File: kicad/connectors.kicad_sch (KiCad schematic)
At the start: 3 parts, among them J2 Conn_02x05_Odd_Even, J3 Conn_01x05, J4 Conn_01x05

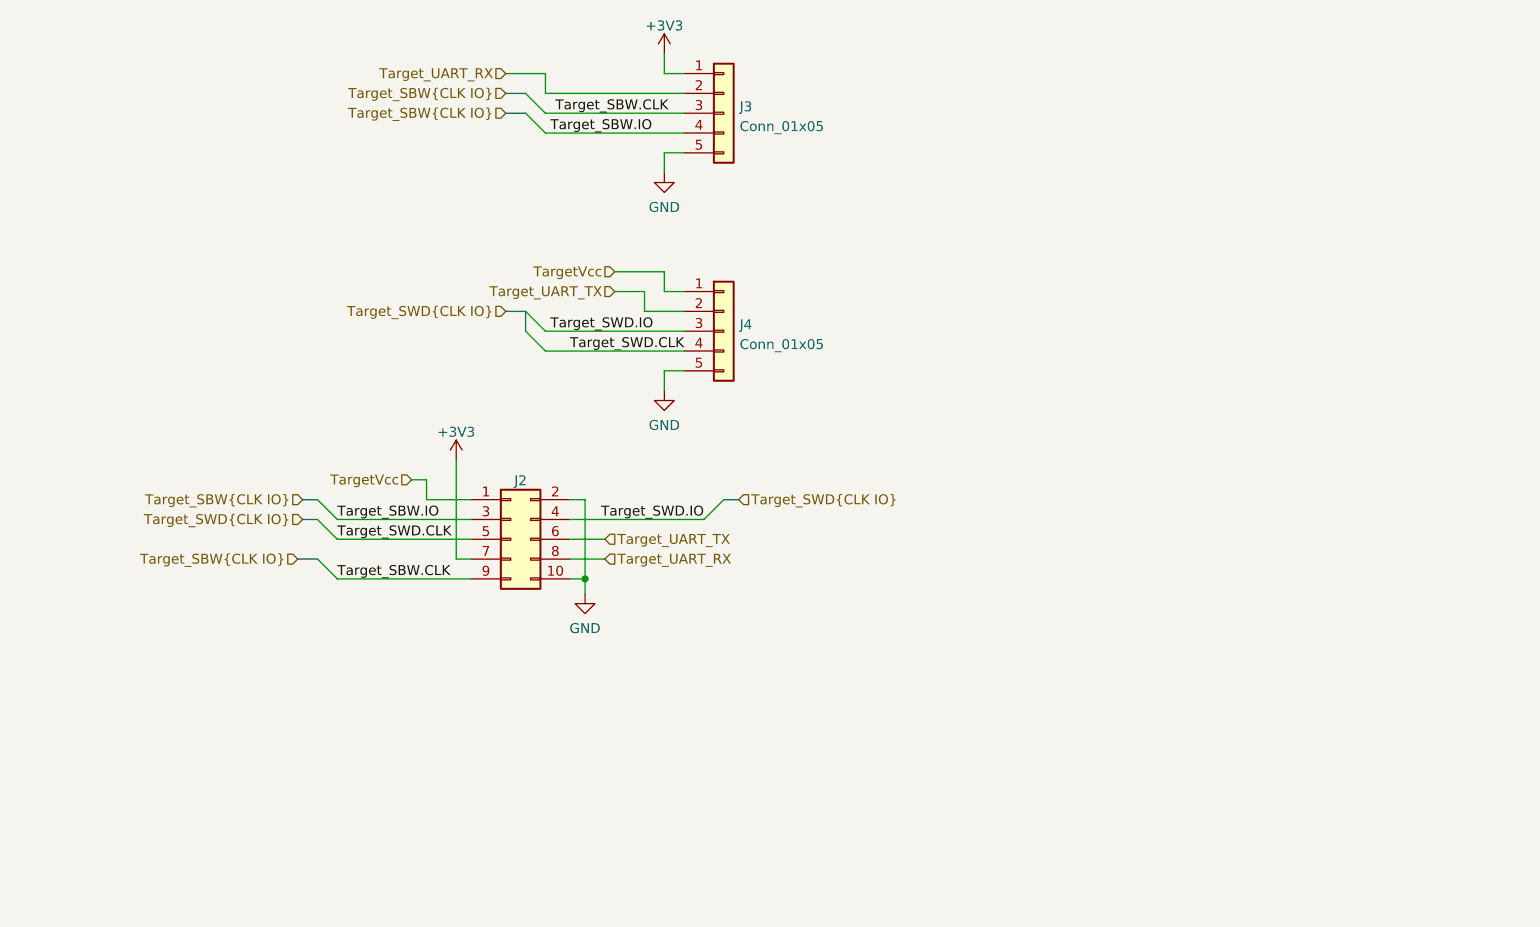
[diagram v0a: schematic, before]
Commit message: add fourth level converter for simultaneous programming + TX/RX
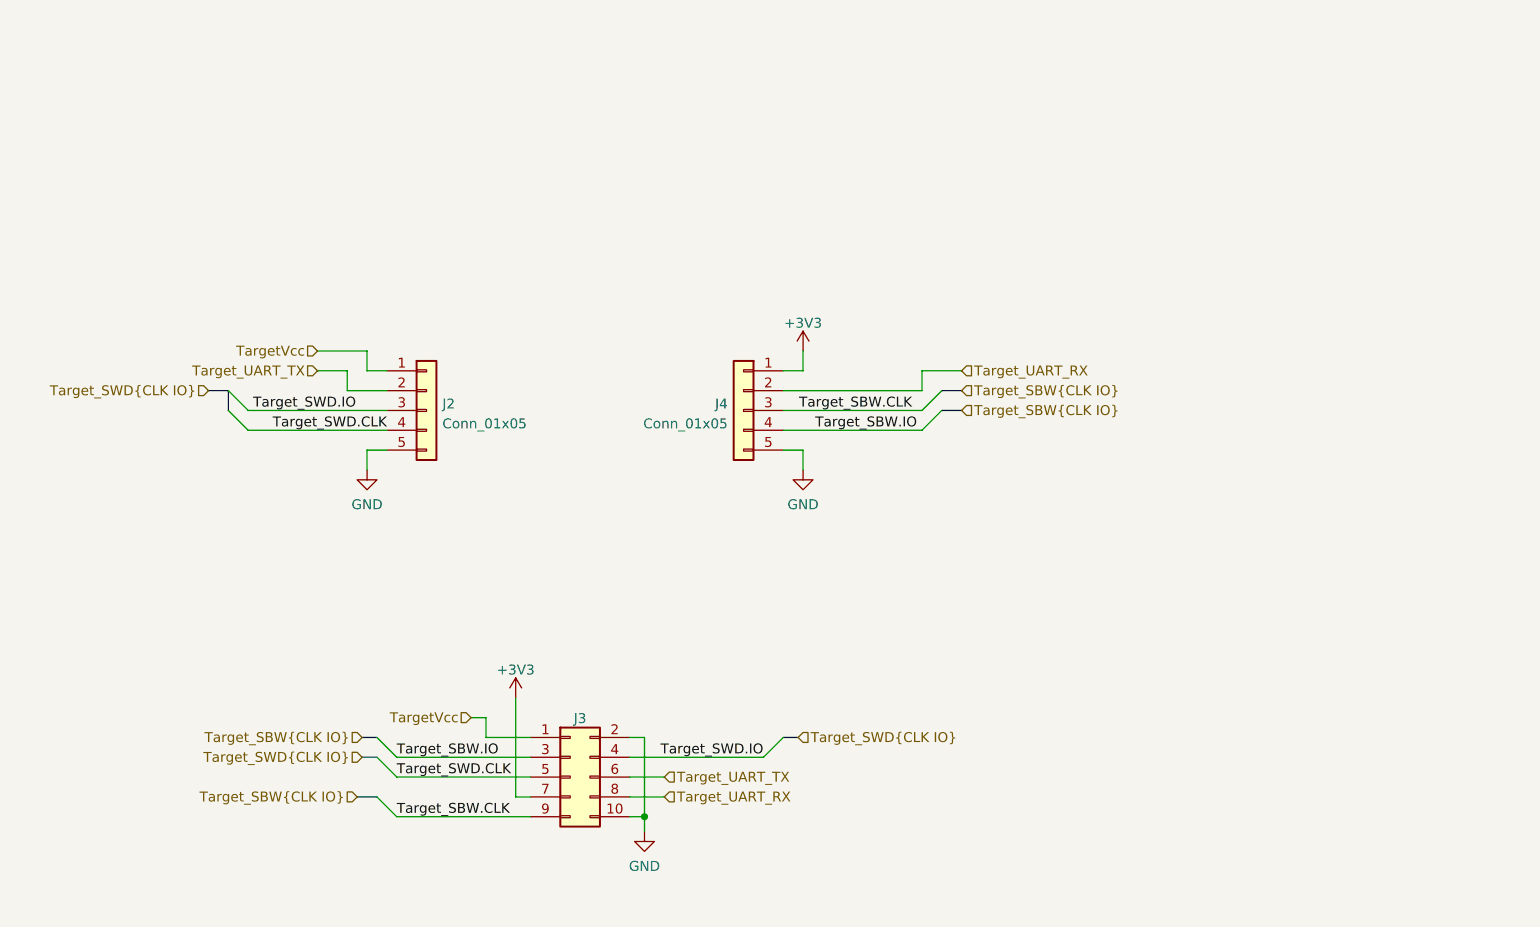
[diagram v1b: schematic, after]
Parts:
- renumbered J4 to J2, J2 to J3, J3 to J4
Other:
- moved on the sheet: J2, J3, J4

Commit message: replace target supply diode with analog switch
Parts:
- removed J2, J4: Conn_01x05, riotee:PinHeader_1x05_P2.54mm_Plain, symbol Connector_Generic:Conn_01x05
- added C28: 0.1u, Capacitor_SMD:C_0402_1005Metric, symbol Device:C
- added J2, J4: Conn_01x07, riotee:PinHeader_1x07_P2.54mm_Plain, symbol Connector_Generic:Conn_01x07
- added R27: 12R, Resistor_SMD:R_0402_1005Metric, symbol Device:R
- added U9: TS5A3166YZP, riotee:TI_YZP0005, symbol riotee:TS5A3166YZP
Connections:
- net +3V3: now also C28.1, J4.1 (Pin_1), U9.A2 (V+)
- net GND: now also C28.2, J2.7 (Pin_7), J4.7 (Pin_7), R27.1, U9.C1 (GND)
- net TargetVcc: now also J2.1 (Pin_1), U9.A1
- net Target_SBW.CLK: now also J4.5 (Pin_5)
- net Target_SBW.IO: now also J4.6 (Pin_6)
- net Target_SWD.CLK: now also J2.6 (Pin_6)
- net Target_SWD.IO: now also J2.5 (Pin_5)
- net Target_UART_RX: now also J4.4 (Pin_4)
- net Target_UART_TX: now also J2.4 (Pin_4)
- new net +2V1: U9.B1
- new net PiGpio0: J2.2 (Pin_2)
- new net PiGpio1: J2.3 (Pin_3)
- new net PiGpio2: J4.3 (Pin_3)
- new net PiGpio3: J4.2 (Pin_2)
- new net TargetPowerEnable: R27.2, U9.C2

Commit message: add MPNs in schematics
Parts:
- C28: MPN (none) -> CL05A104KA5NNNC
- J3: MPN (none) -> AWHW 10G-SMD
- R27: MPN (none) -> RMCF0402FT12R0
- U9: MPN (none) -> TS5A3166YZP
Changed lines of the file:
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@@
+      (effects (font (size 1.27 1.27)) hide)
+    )
+    (property "MPN" "AWHW 10G-SMD" (id 4) (at 142.875 130.81 0)
       (effects (font (size 1.27 1.27)) hide)
     )
@@
       (effects (font (size 1.27 1.27)) hide)
     )
+    (property "MPN" "TS5A3166YZP" (id 4) (at 238.76 125.73 0)
+      (effects (font (size 1.27 1.27)) hide)
+    )
     (pin "A1")
     (pin "A2")
@@
       (effects (font (size 1.27 1.27)) hide)
     )
+    (property "MPN" "CL05A104KA5NNNC" (id 4) (at 247.65 111.76 0)
+      (effects (font (size 1.27 1.27)) hide)
+    )
     (pin "1")
     (pin "2")
@@
       (effects (font (size 1.27 1.27)) hide)
     )
+    (property "MPN" "RMCF0402FT12R0" (id 4) (at 226.06 135.89 0)
+      (effects (font (size 1.27 1.27)) hide)
+    )

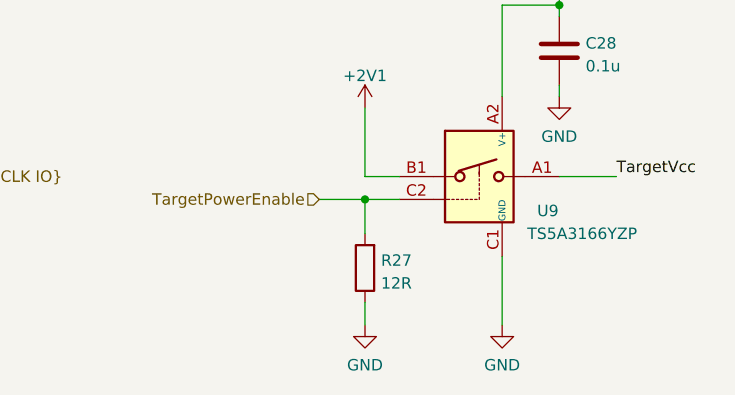
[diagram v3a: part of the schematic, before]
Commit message: fix pulldown value
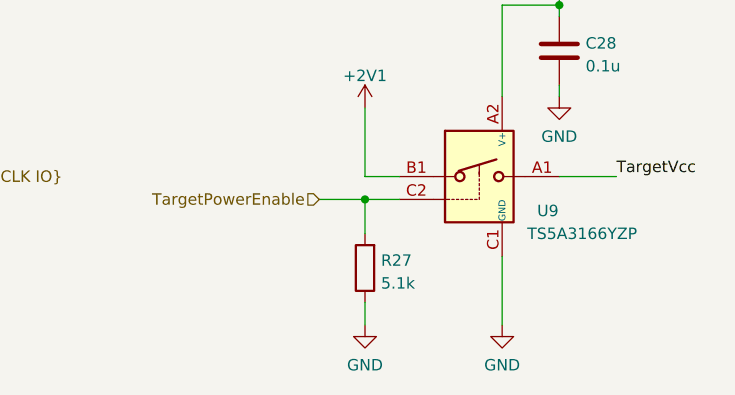
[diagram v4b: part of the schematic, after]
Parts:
- R27: value 12R -> 5.1k
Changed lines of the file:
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@@
       (effects (font (size 1.27 1.27)) (justify right))
     )
-    (property "Value" "12R" (id 1) (at 227.838 137.5922 0)
+    (property "Value" "5.1k" (id 1) (at 227.838 137.5922 0)
       (effects (font (size 1.27 1.27)) (justify right))
     )

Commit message: update footprints and add component description to BOM
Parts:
- J2, J4: now left out of the parts list
- R27: MPN RMCF0402FT12R0 -> CR0402-FX-5101GLF
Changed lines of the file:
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@@
   )
   (symbol (lib_id "Connector_Generic:Conn_01x07") (at 124.46 81.28 0) (unit 1)
-    (in_bom yes) (on_board yes) (fields_autoplaced)
+    (in_bom no) (on_board yes) (fields_autoplaced)
     (property "Reference" "J2" (id 0) (at 126.492 80.4453 0)
       (effects (font (size 1.27 1.27)) (justify left))
@@
       (effects (font (size 1.27 1.27)) hide)
     )
+    (property "Description" "1-Ohm SPST switch" (id 5) (at 238.76 125.73 0)
+      (effects (font (size 1.27 1.27)) hide)
+    )
     (pin "A1")
     (pin "A2")
@@
   )
   (symbol (lib_id "Connector_Generic:Conn_01x07") (at 165.1 81.28 0) (mirror y) (unit 1)
-    (in_bom yes) (on_board yes) (fields_autoplaced)
+    (in_bom no) (on_board yes) (fields_autoplaced)
     (property "Reference" "J4" (id 0) (at 165.1 68.6902 0))
     (property "Value" "Conn_01x07" (id 1) (at 165.1 71.2271 0))
@@
       (effects (font (size 1.27 1.27)) hide)
     )
+    (property "Description" "Cap, 0402, X5R/X7R, 10V" (id 5) (at 247.65 111.76 0)
+      (effects (font (size 1.27 1.27)) hide)
+    )
     (pin "1")
     (pin "2")
@@
       (effects (font (size 1.27 1.27)) hide)
     )
-    (property "MPN" "RMCF0402FT12R0" (id 4) (at 226.06 135.89 0)
-      (effects (font (size 1.27 1.27)) hide)
-    )
+    (property "MPN" "CR0402-FX-5101GLF" (id 4) (at 226.06 135.89 0)
+      (effects (font (size 1.27 1.27)) hide)
+    )
+    (property "Description" "Res, 0402, 1%" (id 5) (at 226.06 135.89 0)
+      (effects (font (size 1.27 1.27)) hide)
+    )

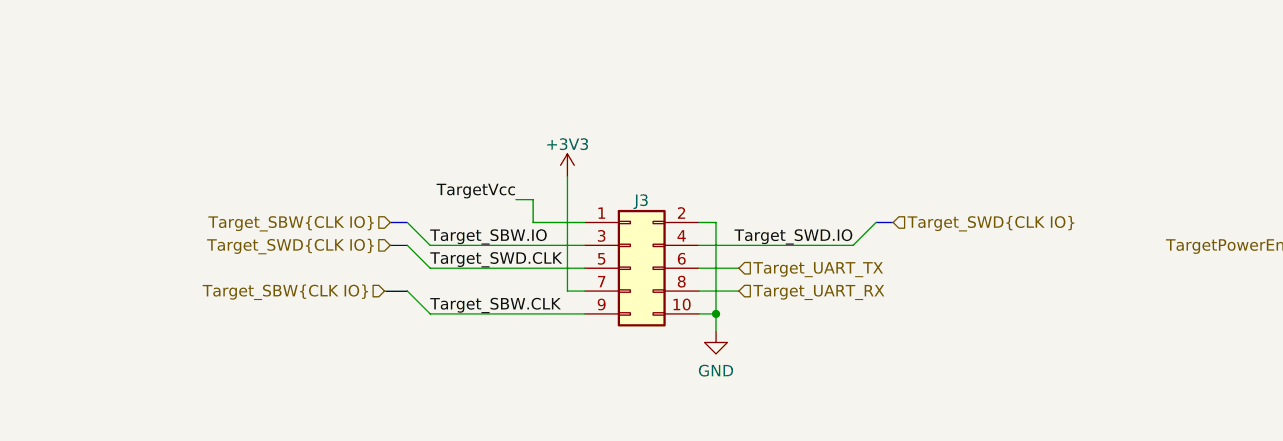
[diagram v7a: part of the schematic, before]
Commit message: migrate project to kicad 7
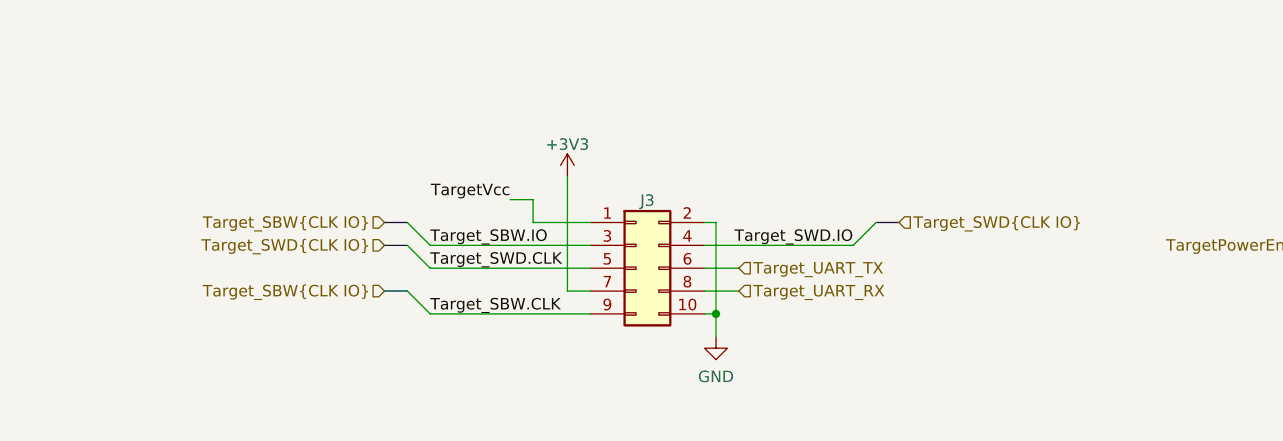
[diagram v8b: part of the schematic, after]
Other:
- moved on the sheet: J3
